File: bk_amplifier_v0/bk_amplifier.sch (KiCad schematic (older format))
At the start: 11 parts, among them U1 AD745

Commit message: new bk8103 model
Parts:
- removed C3: 500p, symbol Device:C
- removed C4: 3.2n, symbol Device:C
- removed I4: 0, symbol pspice:ISOURCE
- removed R3: 0.1, symbol Device:R
- removed R4: 2.5G, symbol Device:R
- added J1, J2: Conn_Coaxial, symbol Connector:Conn_Coaxial
- U1: symbol opamp:AD745 -> bk_amplifier-rescue:AD745-opamp; Spice_Lib_File ad745\\ad745.cir -> bk_amplifier-cache.lib
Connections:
- net labels added: in, retro
- net labels removed: hydro, in-, sig, wire
- wire segments 37 -> 30
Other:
- note added: "gain is given by Cin/C1\nC1 in polystyren"
- note removed: "B&K 8103:\n3.7nF 2.5GOhm with its wire\n29uV/Pa (0.1pC/Pa)\n"
- note removed: "gain is given by Cinput/C1\nC1 in polystyren"
- moved on the sheet: C1, R1, R2, V1, V2

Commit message: keeping opamp near the project, hope it helps to share
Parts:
- removed U1: AD745, Package_SO:SOIC-16W_7.5x10.3mm_P1.27mm, symbol bk_amplifier-rescue:AD745-opamp
- added U1: AD745, Package_SO:SOIC-16W_7.5x10.3mm_P1.27mm, symbol opamp:AD745
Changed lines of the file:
@@
 Wire Wire Line
 	5300 3200 5300 3250
-$Comp
-L bk_amplifier-rescue:AD745-opamp U1
-U 1 1 5DA595E3
-P 6450 4650
-F 0 "U1" H 6794 4696 50  0000 L CNN
-F 1 "AD745" H 6794 4605 50  0000 L CNN
-F 2 "Package_SO:SOIC-16W_7.5x10.3mm_P1.27mm" H 6750 4400 50  0001 C CNN
-F 3 "" H 6750 4400 50  0001 C CNN
-F 4 "X" H 6550 4500 50  0001 C CNN "Spice_Primitive"
-F 5 "AD745" H 6550 4500 50  0001 C CNN "Spice_Model"
-F 6 "Y" H 6550 4500 50  0001 C CNN "Spice_Netlist_Enabled"
-F 7 "bk_amplifier-cache.lib" H 6550 4500 50  0001 C CNN "Spice_Lib_File"
-	1    6450 4650
-	1    0    0    1
-$EndComp
 Wire Wire Line
 	4650 4750 6150 4750
@@
 Connection ~ 7200 4650
 $Comp
-L power:GND #PWR?
+L power:GND #PWR0103
 U 1 1 5DA6EEA2
 P 7500 5000
-F 0 "#PWR?" H 7500 4750 50  0001 C CNN
+F 0 "#PWR0103" H 7500 4750 50  0001 C CNN
 F 1 "GND" H 7505 4827 50  0000 C CNN
 F 2 "" H 7500 5000 50  0001 C CNN
@@
 	-1   0    0    -1
 $EndComp
+$Comp
+L opamp:AD745 U1
+U 1 1 5DA6D311
+P 6450 4650
+F 0 "U1" H 6450 4450 50  0000 L CNN
+F 1 "AD745" H 6450 4850 50  0000 L CNN
+F 2 "Package_SO:SOIC-16W_7.5x10.3mm_P1.27mm" H 6750 4400 50  0001 C CNN
+F 3 "OPAMP\\ad745\\AD745.pdf" H 6750 4400 50  0001 C CNN
+F 4 "X" H 6550 4500 50  0001 C CNN "Spice_Primitive"
+F 5 "AD745" H 6550 4500 50  0001 C CNN "Spice_Model"
+F 6 "Y" H 6550 4500 50  0001 C CNN "Spice_Netlist_Enabled"
+F 7 "OPAMP\\ad745\\ad745.cir" H 6550 4500 50  0001 C CNN "Spice_Lib_File"
+F 8 "5 3 13 6 12" H 6794 4559 50  0001 L CNN "Spice_Node_Sequence"
+	1    6450 4650
+	1    0    0    -1
+$EndComp
 $EndSCHEMATC

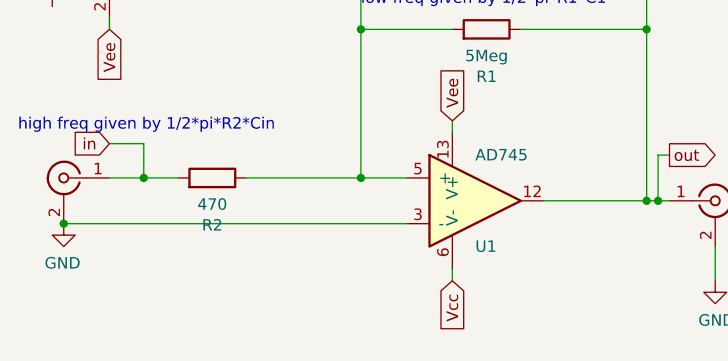
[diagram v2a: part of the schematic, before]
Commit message: 2 models for the B&K8103: charge or voltage source, use the voltage one for now
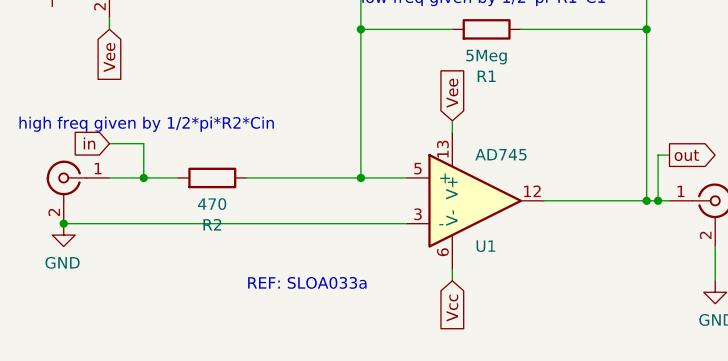
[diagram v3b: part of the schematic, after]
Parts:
- J1: Spice_Model BK8103 -> BK8103_V
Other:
- note added: "REF: SLOA033a"
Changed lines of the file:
@@
 F 3 " ~" H 4650 4550 50  0001 C CNN
 F 4 "X" H 4650 4550 50  0001 C CNN "Spice_Primitive"
-F 5 "BK8103" H 4650 4550 50  0001 C CNN "Spice_Model"
+F 5 "BK8103_V" H 4650 4550 50  0001 C CNN "Spice_Model"
 F 6 "Y" H 4650 4550 50  0001 C CNN "Spice_Netlist_Enabled"
 F 7 "bk8103.cir" H 4650 4550 50  0001 C CNN "Spice_Lib_File"
@@
 	1    0    0    -1
 $EndComp
+Text Notes 5450 5050 0    50   ~ 0
+REF: SLOA033a
 $EndSCHEMATC
